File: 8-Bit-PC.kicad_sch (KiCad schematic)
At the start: 0 parts

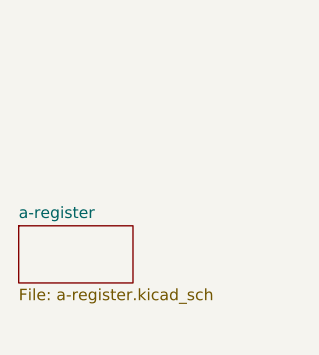
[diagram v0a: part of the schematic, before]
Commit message: Made the a-register and edited it to make it work for the b-register
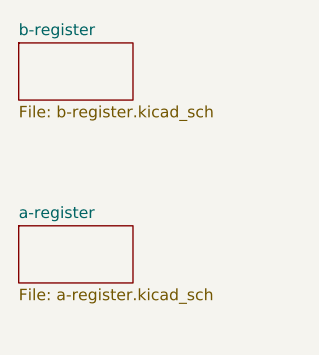
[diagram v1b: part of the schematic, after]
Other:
- added sheet b-register (b-register.kicad_sch)
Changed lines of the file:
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@@
 	(paper "A4")
+	(sheet
+		(at 22.86 115.57)
+		(size 12.7 6.35)
+		(exclude_from_sim no)
+		(in_bom yes)
+		(on_board yes)
+		(dnp no)
+		(fields_autoplaced yes)
+		(stroke
+			(width 0.1524)
+			(type solid)
+		)
+		(fill
+			(color 0 0 0 0.0000)
+		)
+		(property "Sheetname" "b-register"
+			(at 22.86 114.8584 0)
+			(effects
+				(font
+					(size 1.27 1.27)
+				)
+				(justify left bottom)
+			)
+		)
+		(property "Sheetfile" "b-register.kicad_sch"
+			(at 22.86 122.5046 0)
+			(effects
+				(font
+					(size 1.27 1.27)
+				)
+				(justify left top)
+			)
+		)
+		(instances
+			(project "8-Bit-PC"
+				(path "/48633dea-2de9-4b6f-aeff-2ee54233f918"
+					(page "4")
+				)
+			)
+		)
+	)
 	(sheet
 		(at 22.86 135.89)

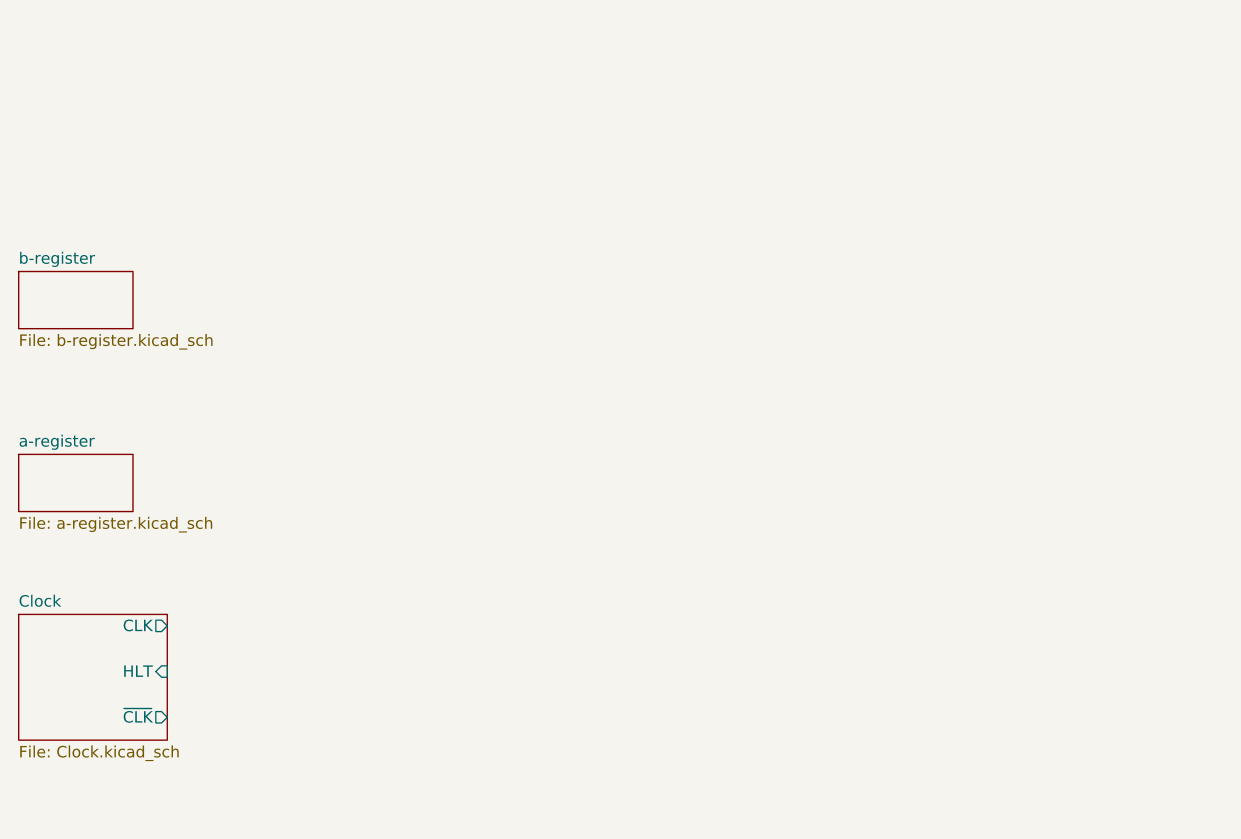
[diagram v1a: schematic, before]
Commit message: Added the ALU and flags register schematic.
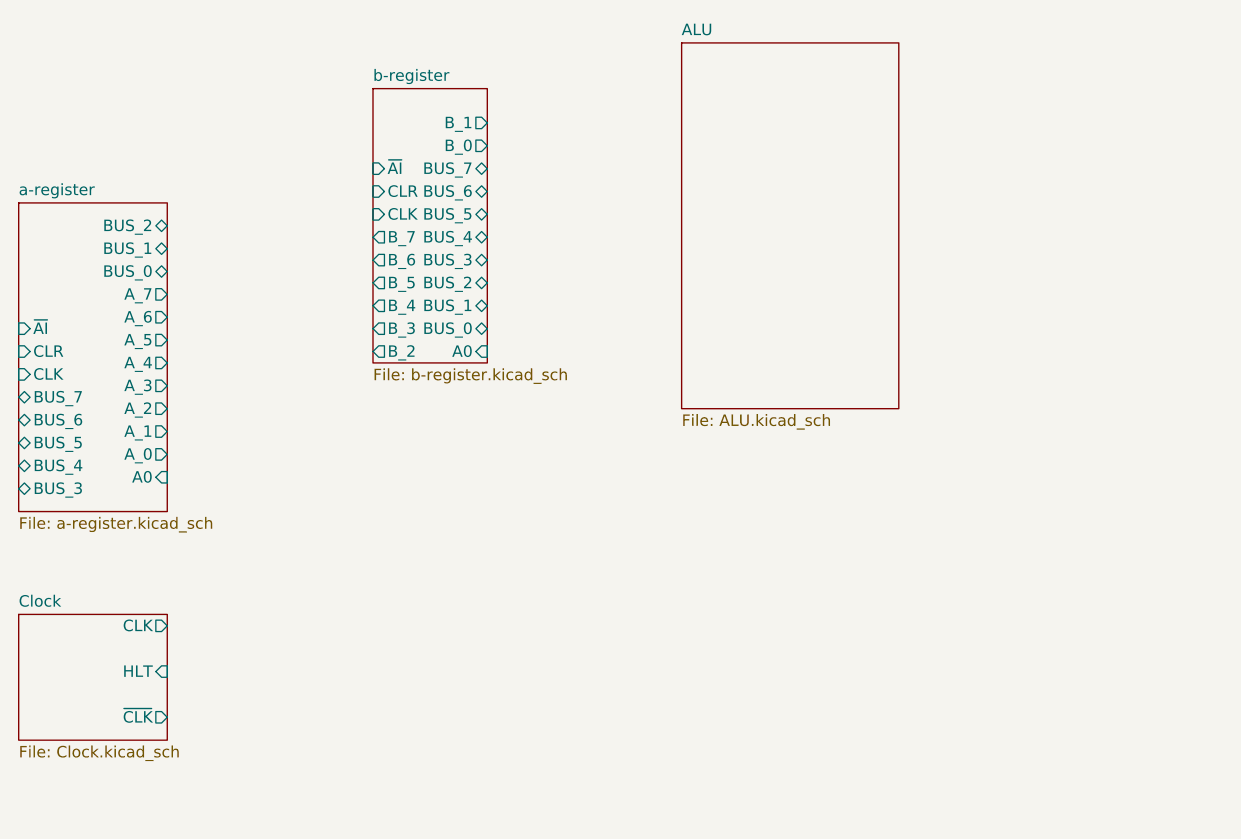
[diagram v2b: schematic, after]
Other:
- added sheet ALU (ALU.kicad_sch)
- sheet a-register ports: added A0, A_0, A_1, A_2, A_3, A_4, A_5, A_6, A_7, BUS_0, BUS_1, BUS_2, BUS_3, BUS_4, BUS_5, BUS_6, BUS_7, CLK, CLR, ~{AI}; removed none
- sheet b-register ports: added A0, BUS_0, BUS_1, BUS_2, BUS_3, BUS_4, BUS_5, BUS_6, BUS_7, B_0, B_1, B_2, B_3, B_4, B_5, B_6, B_7, CLK, CLR, ~{AI}; removed none
- title: (none) -> 8 bit PC

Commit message: set up the MAR module and got started on the RAM module
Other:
- added sheet MAR (mar.kicad_sch)
- added sheet RAM (ram.kicad_sch)
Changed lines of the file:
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@@
+	)
+	(sheet
+		(at 59.69 142.24)
+		(size 21.59 31.75)
+		(exclude_from_sim no)
+		(in_bom yes)
+		(on_board yes)
+		(dnp no)
+		(fields_autoplaced yes)
+		(stroke
+			(width 0.1524)
+			(type solid)
+		)
+		(fill
+			(color 0 0 0 0.0000)
+		)
+		(property "Sheetname" "MAR"
+			(at 59.69 141.5284 0)
+			(effects
+				(font
+					(size 1.27 1.27)
+				)
+				(justify left bottom)
+			)
+		)
+		(property "Sheetfile" "mar.kicad_sch"
+			(at 59.69 174.5746 0)
+			(effects
+				(font
+					(size 1.27 1.27)
+				)
+				(justify left top)
+			)
+		)
+		(instances
+			(project "8-Bit-PC"
+				(path "/48633dea-2de9-4b6f-aeff-2ee54233f918"
+					(page "6")
+				)
+			)
+		)
 	)
 	(sheet
@@
 				)
 			)
+		)
+	)
+	(sheet
+		(at 133.35 152.4)
+		(size 12.7 20.32)
+		(exclude_from_sim no)
+		(in_bom yes)
+		(on_board yes)
+		(dnp no)
+		(fields_autoplaced yes)
+		(stroke
+			(width 0.1524)
+			(type solid)
+		)
+		(fill
+			(color 0 0 0 0.0000)
+		)
+		(property "Sheetname" "RAM"
+			(at 133.35 151.6884 0)
+			(effects
+				(font
+					(size 1.27 1.27)
+				)
+				(justify left bottom)
+			)
+		)
+		(property "Sheetfile" "ram.kicad_sch"
+			(at 133.35 173.3046 0)
+			(effects
+				(font
+					(size 1.27 1.27)
+				)
+				(justify left top)
+			)
+		)
+		(instances
+			(project "8-Bit-PC"
+				(path "/48633dea-2de9-4b6f-aeff-2ee54233f918"
+					(page "7")
+				)
+			)

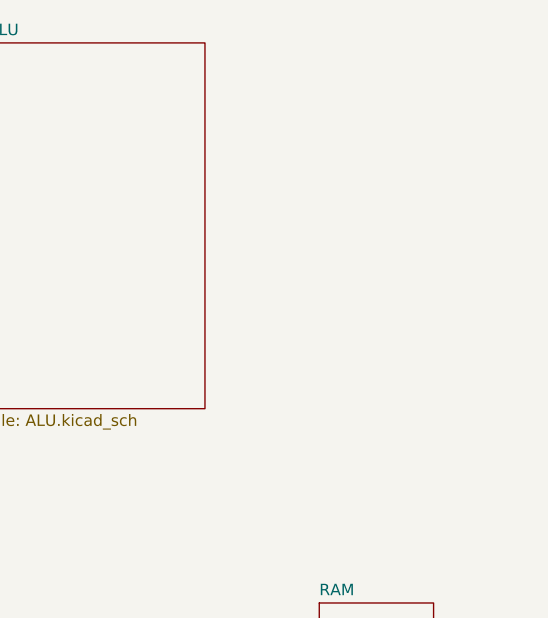
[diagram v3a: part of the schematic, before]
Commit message: Added the program counter
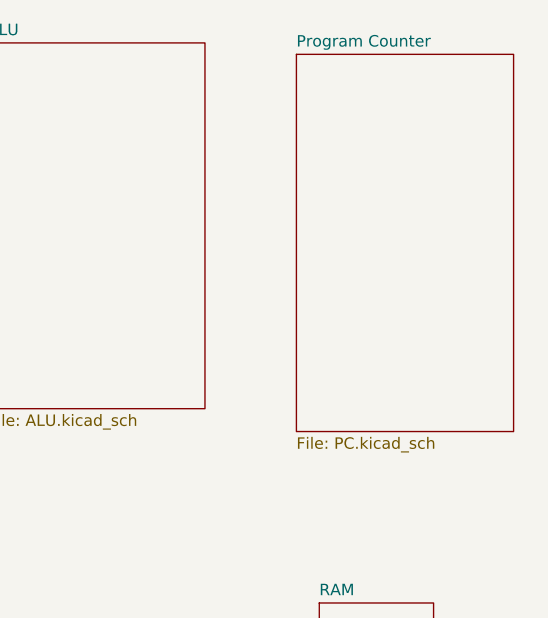
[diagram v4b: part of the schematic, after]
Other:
- added sheet Program Counter (PC.kicad_sch)
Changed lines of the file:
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@@
+	)
+	(sheet
+		(at 130.81 91.44)
+		(size 24.13 41.91)
+		(exclude_from_sim no)
+		(in_bom yes)
+		(on_board yes)
+		(dnp no)
+		(fields_autoplaced yes)
+		(stroke
+			(width 0.1524)
+			(type solid)
+		)
+		(fill
+			(color 0 0 0 0.0000)
+		)
+		(property "Sheetname" "Program Counter"
+			(at 130.81 90.7284 0)
+			(effects
+				(font
+					(size 1.27 1.27)
+				)
+				(justify left bottom)
+			)
+		)
+		(property "Sheetfile" "PC.kicad_sch"
+			(at 130.81 133.9346 0)
+			(effects
+				(font
+					(size 1.27 1.27)
+				)
+				(justify left top)
+			)
+		)
+		(instances
+			(project "8-Bit-PC"
+				(path "/48633dea-2de9-4b6f-aeff-2ee54233f918"
+					(page "8")
+				)
+			)
+		)
 	)
 	(sheet
